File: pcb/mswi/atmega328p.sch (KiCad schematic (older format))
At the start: 49 parts, among them J301 AVR-ISP-6, J302 USART, J303 I2C, Q301 BC856, U301 ATmega328PB-AU, Y301 16MHz

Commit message: routing: wip
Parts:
- removed J301: AVR-ISP-6, Connector_IDC:IDC-Header_2x03_P2.54mm_Vertical, symbol Connector:AVR-ISP-6
- added J301: ISP, Connector_PinHeader_2.54mm:PinHeader_1x06_P2.54mm_Vertical, symbol Connector_Generic:Conn_01x06
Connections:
- net +5V: now also J303.1 (Pin_1), J301.2 (Pin_2); no longer J303.2 (Pin_2)
- net BUZZER: now also U301.12 (PB0); no longer U301.14 (PB2)
- net GND: now also J303.2 (Pin_2), J301.1 (Pin_1); no longer J303.1 (Pin_1)
- net MCP_INT: now also U301.14 (PB2); no longer U301.13 (PB1)
- net MCP_SS: now also U301.13 (PB1); no longer U301.12 (PB0)
- net SPI_MISO: no longer R301.1, R306.1, U301.16 (PB4)
- net SPI_MOSI: no longer R302.1, R305.1, U301.15 (PB3)
- net SPI_SCK: no longer R303.1, R307.1, U301.17 (PB5)
- net at R301.2: now also J301.6 (Pin_6)
- net at R303.2: now also J301.4 (Pin_4)
- net at R302.2: now also J301.5 (Pin_5)
- net at R304.2: now also J301.3 (Pin_3)
- new net SPI_MISO_: R302.1, R306.1, U301.16 (PB4)
- new net SPI_MOSI_: R301.1, R305.1, U301.15 (PB3)
- new net SPI_SCK_: R303.1, R307.1, U301.17 (PB5)
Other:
- moved on the sheet: C303, C308, R301, R302, R303, R304
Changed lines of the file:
@@
 Text HLabel 5950 2750 2    60   Output ~ 0
 SPI_MOSI
-Text HLabel 5950 2450 2    60   Output ~ 0
+Text HLabel 5950 2550 2    60   Output ~ 0
 MCP_SS
-Text HLabel 5950 2550 2    60   Input ~ 0
+Text HLabel 5950 2650 2    60   Input ~ 0
 MCP_INT
 Text Label 4550 3950 0    60   ~ 0
@@
 	4450 4150 4550 4150
 Wire Wire Line
-	5950 2450 4450 2450
+	5950 2550 4450 2550
 Wire Wire Line
 	4450 2750 5500 2750
@@
 	4450 2950 5500 2950
 Wire Wire Line
-	4450 2550 5950 2550
+	4450 2650 5950 2650
 Wire Wire Line
 	4550 3350 4450 3350
@@
 	1650 3550 1650 3500
 Text Label 4550 2850 0    60   ~ 0
-SPI_MISO
+SPI_MISO_
 Text Label 4550 2750 0    60   ~ 0
-SPI_MOSI
+SPI_MOSI_
 Text Label 4550 2950 0    60   ~ 0
-SPI_SCK
+SPI_SCK_
 Wire Wire Line
 	4450 4850 4550 4850
@@
 	3150 2750 3150 2800
 Wire Wire Line
-	4550 2650 4450 2650
+	4550 2450 4450 2450
+Text Label 4550 2650 0    60   ~ 0
+MCP_INT
 Text Label 4550 2550 0    60   ~ 0
-MCP_INT
-Text Label 4550 2450 0    60   ~ 0
 MCP_SS
-$Comp
-L Connector:AVR-ISP-6 J301
-U 1 1 5D9F84CC
-P 9200 2550
-F 0 "J301" H 8900 2400 50  0000 R CNN
-F 1 "AVR-ISP-6" H 8900 2300 50  0000 R CNN
-F 2 "Connector_IDC:IDC-Header_2x03_P2.54mm_Vertical" V 8950 2600 50  0001 C CNN
-F 3 " ~" H 7925 2000 50  0001 C CNN
-	1    9200 2550
-	-1   0    0    -1
-$EndComp
-Text Label 7750 2450 0    60   ~ 0
-SPI_MOSI
-Text Label 7750 2350 0    60   ~ 0
-SPI_MISO
-Text Label 7750 2550 0    60   ~ 0
-SPI_SCK
-Text Label 7750 2650 0    60   ~ 0
+Text Label 7750 1850 0    60   ~ 0
+SPI_MOSI_
+Text Label 7750 1950 0    60   ~ 0
+SPI_MISO_
+Text Label 7750 2050 0    60   ~ 0
+SPI_SCK_
+Text Label 7750 2150 0    60   ~ 0
 RESET
 Text Notes 550  700  0    50   ~ 0
@@
 L Device:R_Small R301
 U 1 1 5DA1621D
-P 8500 2350
-F 0 "R301" V 8550 2050 50  0000 L CNN
-F 1 "100R" V 8550 2450 50  0000 L CNN
-F 2 "Resistor_SMD:R_0805_2012Metric_Pad1.15x1.40mm_HandSolder" H 8500 2350 50  0001 C CNN
-F 3 "" H 8500 2350 50  0001 C CNN
-	1    8500 2350
-	0    -1   -1   0
-$EndComp
-Wire Wire Line
-	8800 2350 8600 2350
-Wire Wire Line
-	8600 2450 8800 2450
-Wire Wire Line
-	8800 2550 8600 2550
+P 8500 1850
+F 0 "R301" V 8550 1550 50  0000 L CNN
+F 1 "100R" V 8550 1950 50  0000 L CNN
+F 2 "Resistor_SMD:R_0805_2012Metric_Pad1.15x1.40mm_HandSolder" H 8500 1850 50  0001 C CNN
+F 3 "" H 8500 1850 50  0001 C CNN
+	1    8500 1850
+	0    -1   -1   0
+$EndComp
+Wire Wire Line
+	8800 1850 8600 1850
+Wire Wire Line
+	8600 1950 8800 1950
+Wire Wire Line
+	8800 2050 8600 2050
 $Comp
 L Device:R_Small R302
 U 1 1 5DA1FCA0
-P 8500 2450
-F 0 "R302" V 8550 2150 50  0000 L CNN
-F 1 "100R" V 8550 2550 50  0000 L CNN
-F 2 "Resistor_SMD:R_0805_2012Metric_Pad1.15x1.40mm_HandSolder" H 8500 2450 50  0001 C CNN
-F 3 "" H 8500 2450 50  0001 C CNN
-	1    8500 2450
+P 8500 1950
+F 0 "R302" V 8550 1650 50  0000 L CNN
+F 1 "100R" V 8550 2050 50  0000 L CNN
+F 2 "Resistor_SMD:R_0805_2012Metric_Pad1.15x1.40mm_HandSolder" H 8500 1950 50  0001 C CNN
+F 3 "" H 8500 1950 50  0001 C CNN
+	1    8500 1950
 	0    -1   -1   0
 $EndComp
@@
 L Device:R_Small R303
 U 1 1 5DA1FDAC
-P 8500 2550
-F 0 "R303" V 8550 2250 50  0000 L CNN
-F 1 "100R" V 8550 2650 50  0000 L CNN
-F 2 "Resistor_SMD:R_0805_2012Metric_Pad1.15x1.40mm_HandSolder" H 8500 2550 50  0001 C CNN
-F 3 "" H 8500 2550 50  0001 C CNN
-	1    8500 2550
-	0    -1   -1   0
-$EndComp
-Wire Wire Line
-	7750 2350 8400 2350
-Wire Wire Line
-	7750 2450 8400 2450
-Wire Wire Line
-	7750 2550 8400 2550
+P 8500 2050
+F 0 "R303" V 8550 1750 50  0000 L CNN
+F 1 "100R" V 8550 2150 50  0000 L CNN
+F 2 "Resistor_SMD:R_0805_2012Metric_Pad1.15x1.40mm_HandSolder" H 8500 2050 50  0001 C CNN
+F 3 "" H 8500 2050 50  0001 C CNN
+	1    8500 2050
+	0    -1   -1   0
+$EndComp
+Wire Wire Line
+	7750 1850 8400 1850
+Wire Wire Line
+	7750 1950 8400 1950
+Wire Wire Line
+	7750 2050 8400 2050
 $Comp
 L Device:R_Small R304
 U 1 1 5DA29770
-P 8500 2650
-F 0 "R304" V 8550 2350 50  0000 L CNN
-F 1 "100R" V 8550 2750 50  0000 L CNN
-F 2 "Resistor_SMD:R_0805_2012Metric_Pad1.15x1.40mm_HandSolder" H 8500 2650 50  0001 C CNN
-F 3 "" H 8500 2650 50  0001 C CNN
-	1    8500 2650
-	0    -1   -1   0
-$EndComp
-Wire Wire Line
-	8800 2650 8600 2650
-Wire Wire Line
-	7750 2650 8400 2650
+P 8500 2150
+F 0 "R304" V 8550 1850 50  0000 L CNN
+F 1 "100R" V 8550 2250 50  0000 L CNN
+F 2 "Resistor_SMD:R_0805_2012Metric_Pad1.15x1.40mm_HandSolder" H 8500 2150 50  0001 C CNN
+F 3 "" H 8500 2150 50  0001 C CNN
+	1    8500 2150
+	0    -1   -1   0
+$EndComp
+Wire Wire Line
+	8800 2150 8600 2150
+Wire Wire Line
+	7750 2150 8400 2150
 $Comp
 L Device:R_Small R308
@@
 $EndComp
 $Comp
-L power:GND #PWR0307
-U 1 1 5DA3FBA7
-P 9300 3000
-F 0 "#PWR0307" H 9300 2750 50  0001 C CNN
-F 1 "GND" H 9350 2800 50  0000 C CNN
-F 2 "" H 9300 3000 50  0001 C CNN
-F 3 "" H 9300 3000 50  0001 C CNN
-	1    9300 3000
-	1    0    0    -1
-$EndComp
-Wire Wire Line
-	9300 2950 9300 3000
-$Comp
 L power:+5V #PWR0304
 U 1 1 5DA42480
-P 9300 1900
-F 0 "#PWR0304" H 9300 1750 50  0001 C CNN
-F 1 "+5V" H 9350 2100 50  0000 C CNN
-F 2 "" H 9300 1900 50  0001 C CNN
-F 3 "" H 9300 1900 50  0001 C CNN
-	1    9300 1900
+P 7650 1750
+F 0 "#PWR0304" H 7650 1600 50  0001 C CNN
+F 1 "+5V" H 7700 1950 50  0000 C CNN
+F 2 "" H 7650 1750 50  0001 C CNN
+F 3 "" H 7650 1750 50  0001 C CNN
+	1    7650 1750
 	1    0    0    -1
 $EndComp
@@
 L Device:C_Small C303
 U 1 1 5DAC60E0
-P 9550 2200
-F 0 "C303" H 9650 2200 50  0000 L CNN
-F 1 "100nF" H 9550 2300 50  0000 L CNN
-F 2 "Capacitor_SMD:C_0805_2012Metric_Pad1.15x1.40mm_HandSolder" H 9550 2200 50  0001 C CNN
-F 3 "" H 9550 2200 50  0001 C CNN
-	1    9550 2200
-	1    0    0    -1
-$EndComp
-Wire Wire Line
-	9300 2000 9550 2000
-Wire Wire Line
-	9550 2000 9550 2100
-Connection ~ 9300 2000
-Wire Wire Line
-	9300 2000 9300 2050
+P 7650 2450
+F 0 "C303" H 7750 2450 50  0000 L CNN
+F 1 "100nF" H 7650 2550 50  0000 L CNN
+F 2 "Capacitor_SMD:C_0805_2012Metric_Pad1.15x1.40mm_HandSolder" H 7650 2450 50  0001 C CNN
+F 3 "" H 7650 2450 50  0001 C CNN
+	1    7650 2450
+	1    0    0    -1
+$EndComp
+Wire Wire Line
+	7650 2250 7650 2350
 $Comp
 L power:GND #PWR0305
 U 1 1 5DAD1DDA
-P 9550 2300
-F 0 "#PWR0305" H 9550 2050 50  0001 C CNN
-F 1 "GND" H 9600 2100 50  0000 C CNN
-F 2 "" H 9550 2300 50  0001 C CNN
-F 3 "" H 9550 2300 50  0001 C CNN
-	1    9550 2300
+P 7650 2550
+F 0 "#PWR0305" H 7650 2300 50  0001 C CNN
+F 1 "GND" H 7700 2350 50  0000 C CNN
+F 2 "" H 7650 2550 50  0001 C CNN
+F 3 "" H 7650 2550 50  0001 C CNN
+	1    7650 2550
 	1    0    0    -1
 $EndComp
@@
 L Device:C_Small C308
 U 1 1 5DAD7BBB
-P 7700 4800
-F 0 "C308" H 7800 4800 50  0000 L CNN
-F 1 "100nF" H 7700 4900 50  0000 L CNN
-F 2 "Capacitor_SMD:C_0805_2012Metric_Pad1.15x1.40mm_HandSolder" H 7700 4800 50  0001 C CNN
-F 3 "" H 7700 4800 50  0001 C CNN
-	1    7700 4800
+P 7700 4900
+F 0 "C308" H 7800 4900 50  0000 L CNN
+F 1 "100nF" H 7700 5000 50  0000 L CNN
+F 2 "Capacitor_SMD:C_0805_2012Metric_Pad1.15x1.40mm_HandSolder" H 7700 4900 50  0001 C CNN
+F 3 "" H 7700 4900 50  0001 C CNN
+	1    7700 4900
 	1    0    0    -1
 $EndComp
@@
 Wire Wire Line
 	7750 4500 8150 4500
-Wire Wire Line
-	8600 4800 8600 4700
-Wire Wire Line
-	8600 4700 8800 4700
-Wire Wire Line
-	7700 4700 7700 4600
 $Comp
 L power:GND #PWR0316
 U 1 1 5DAE5F27
-P 7700 4950
-F 0 "#PWR0316" H 7700 4700 50  0001 C CNN
-F 1 "GND" H 7750 4750 50  0000 C CNN
-F 2 "" H 7700 4950 50  0001 C CNN
-F 3 "" H 7700 4950 50  0001 C CNN
-	1    7700 4950
-	1    0    0    -1
-$EndComp
-Wire Wire Line
-	7700 4900 7700 4950
+P 7700 5000
+F 0 "#PWR0316" H 7700 4750 50  0001 C CNN
+F 1 "GND" H 7750 4800 50  0000 C CNN
+F 2 "" H 7700 5000 50  0001 C CNN
+F 3 "" H 7700 5000 50  0001 C CNN
+	1    7700 5000
+	1    0    0    -1
+$EndComp
 $Comp
 L Device:R_Small R312
@@
 	1    0    0    -1
 $EndComp
-Wire Wire Line
-	7700 4250 7700 4600
-Connection ~ 7700 4600
-Wire Wire Line
-	7700 4600 8800 4600
-Wire Wire Line
-	9300 1900 9300 2000
 Text Notes 7150 5450 0    50   ~ 0
 Nota:  Verificar posicionamento dos pinos do OLED e criar conector customizado para ele\n
@@
 Text Label 3150 4450 2    60   ~ 0
 LED3
-Text Label 4550 2650 0    60   ~ 0
+Text Label 4550 2450 0    60   ~ 0
 BUZZER
 Text Label 4550 3350 0    60   ~ 0
@@
 	1    0    0    -1
 $EndComp
+$Comp
+L Connector_Generic:Conn_01x06 J301
+U 1 1 5DF1EE8C
+P 9000 2150
+F 0 "J301" H 8950 1600 50  0000 C CNN
+F 1 "ISP" H 8950 1700 50  0000 C CNN
+F 2 "Connector_PinHeader_2.54mm:PinHeader_1x06_P2.54mm_Vertical" H 9000 2150 50  0001 C CNN
+F 3 "~" H 9000 2150 50  0001 C CNN
+	1    9000 2150
+	1    0    0    1
+$EndComp
+Wire Wire Line
+	7650 2250 8800 2250
+Wire Wire Line
+	7650 1750 7650 2250
+Connection ~ 7650 2250
+Wire Wire Line
+	8600 2350 8600 2450
+Wire Wire Line
+	8800 2350 8600 2350
+$Comp
+L power:GND #PWR0307
+U 1 1 5DA3FBA7
+P 8600 2450
+F 0 "#PWR0307" H 8600 2200 50  0001 C CNN
+F 1 "GND" H 8650 2250 50  0000 C CNN
+F 2 "" H 8600 2450 50  0001 C CNN
+F 3 "" H 8600 2450 50  0001 C CNN
+	1    8600 2450
+	1    0    0    -1
+$EndComp
+Wire Wire Line
+	7700 4250 7700 4700
+Wire Wire Line
+	8600 4600 8800 4600
+Wire Wire Line
+	8600 4600 8600 4800
+Wire Wire Line
+	8800 4700 7700 4700
+Connection ~ 7700 4700
+Wire Wire Line
+	7700 4700 7700 4800
 $EndSCHEMATC

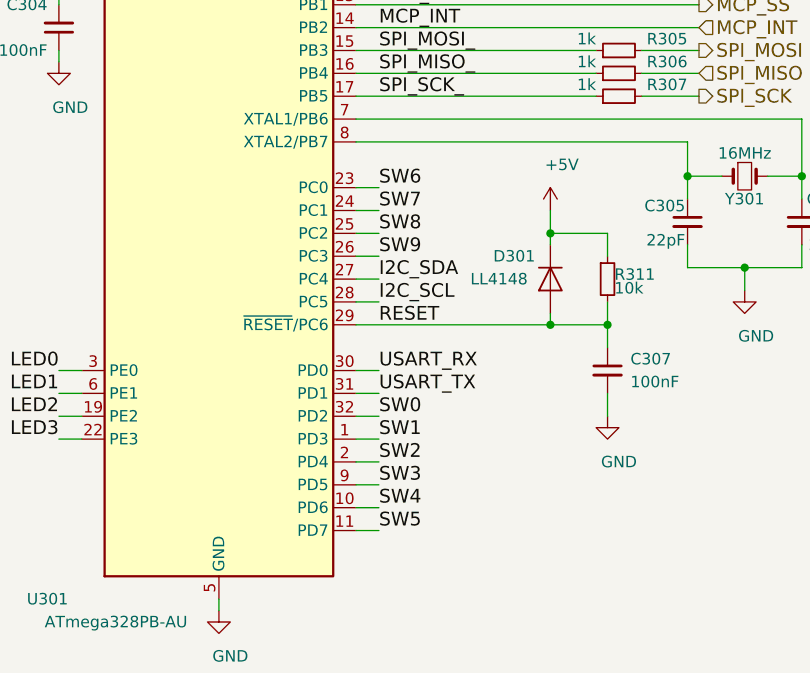
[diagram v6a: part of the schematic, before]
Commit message: Routing done. Needs rework to fabrication
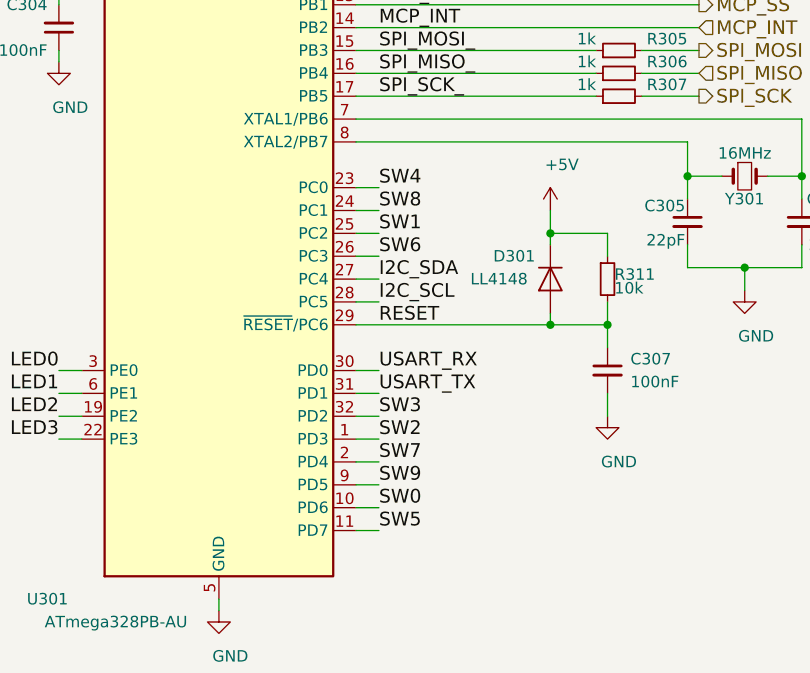
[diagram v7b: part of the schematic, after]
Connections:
- net SW0: now also U301.10 (PD6); no longer U301.32 (PD2)
- net SW1: now also U301.25 (PC2); no longer U301.1 (PD3)
- net SW2: now also U301.1 (PD3); no longer U301.2 (PD4)
- net SW3: now also U301.32 (PD2); no longer U301.9 (PD5)
- net SW4: now also U301.23 (PC0); no longer U301.10 (PD6)
- net SW6: now also U301.26 (PC3); no longer U301.23 (PC0)
- net SW7: now also U301.2 (PD4); no longer U301.24 (PC1)
- net SW8: now also U301.24 (PC1); no longer U301.25 (PC2)
- net SW9: now also U301.9 (PD5); no longer U301.26 (PC3)
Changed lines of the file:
@@
 Text Label 3150 4150 2    60   ~ 0
 LED0
-Text Label 4550 4450 0    60   ~ 0
-SW1
-Text Label 4550 4550 0    60   ~ 0
-SW2
-Text Label 4550 4650 0    60   ~ 0
+Text Label 4550 4350 0    60   ~ 0
 SW3
-Text Label 4550 4750 0    60   ~ 0
+Text Label 4550 3350 0    60   ~ 0
 SW4
 Text Label 4550 4850 0    60   ~ 0
 SW5
-Text Label 4550 4350 0    60   ~ 0
-SW0
 Wire Wire Line
 	3150 4150 3250 4150
@@
 Text Label 4550 2450 0    60   ~ 0
 BUZZER
-Text Label 4550 3350 0    60   ~ 0
+Text Label 4550 3650 0    60   ~ 0
 SW6
+Text Label 4550 4550 0    60   ~ 0
+SW7
 Text Label 4550 3450 0    60   ~ 0
-SW7
-Text Label 4550 3550 0    60   ~ 0
 SW8
-Text Label 4550 3650 0    60   ~ 0
+Text Label 4550 4650 0    60   ~ 0
 SW9
 $Comp
@@
 Wire Wire Line
 	7700 4700 7700 4800
+Text Label 4550 4450 0    60   ~ 0
+SW2
+Text Label 4550 3550 0    60   ~ 0
+SW1
+Text Label 4550 4750 0    60   ~ 0
+SW0
 $EndSCHEMATC
